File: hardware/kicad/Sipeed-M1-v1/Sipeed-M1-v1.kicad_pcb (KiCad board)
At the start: 2 copper layers, 161 parts, among them IC1 TROPIC01_chip, J1 USB_C_, J2 JST Connector, J3 Conn_02x20_Odd_Even, J4 Conn_01x09_Pin, J5 Conn_02x03_Odd_Even, J7 Conn_01x30_Pin, SW1 SW_Push, SW10 SW_Push, SW11 SW_Push, SW12 SW_Push, SW13 SW_Push, SW14 SW_Push, SW15 SW_Push, SW16 SW_Push, SW2 SW_Push, SW3 SW_Push, SW4 SW_Push, SW5 SW_Push, SW6 SW_Push, SW7 SW_Push, SW8 SW_Push, SW9 SW_Push, U1 Sipeed-M1, U2 ESP32-S3-WROOM-1U-N8R8, U3 PAM2401YPADJ, U4 TPS63070RNMR, U5 MCP23017_SO, U6 BQ29700DSER, U7 USBLC6-2SC6, U8 MCP73871

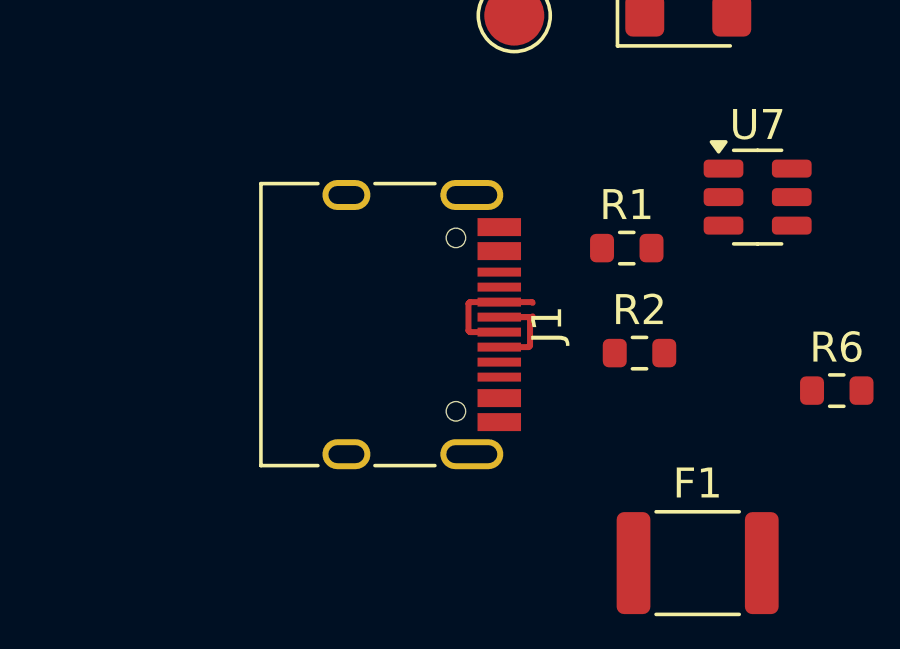
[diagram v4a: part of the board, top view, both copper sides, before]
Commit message: USB-C connector now using SHOU HAN TYPE-C 16PIN 2MD(073)
Adding footprint and 3D model.
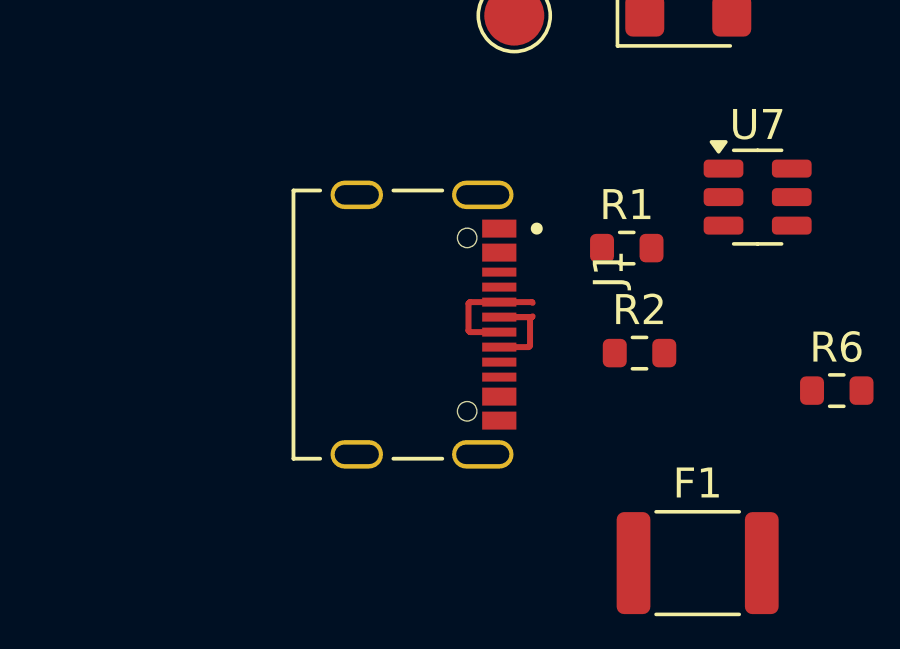
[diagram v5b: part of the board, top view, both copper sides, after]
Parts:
- J1: value USB_C_ -> USB_C; footprint Connector_USB:USB_C_Receptacle_HRO_TYPE-C-31-M-12 -> _M1_FP_lib:SHOUHAN_TYPE-C_16PIN_2MD__073_
- moved J1 0.37 mm to (103.8, 75.0)
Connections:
- J1 pad A8: (no net) -> unconnected-(J1-SBU1-PadA8)
- J1 pad B8: (no net) -> unconnected-(J1-SBU2-PadB8)

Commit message: New FPs for ESP32-S3, R1 and R2. Initial PCB routing.
Opted for ESP32-S3 with embedded PCB antenna.
R1 and R2 are now smaller to fit next to USB-C connector.
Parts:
- removed U6: BQ29700DSER, _M1_FP_lib:BQ29700_SON50P150X150X80-6N
- R1, R15, R2: footprint Resistor_SMD:R_0603_1608Metric -> Resistor_SMD:R_0402_1005Metric
- U2: value ESP32-S3-WROOM-1U-N8R8 -> ESP32-S3-WROOM-1-N4R8; footprint _M1_FP_lib:XCVR_ESP32-S3-WROOM-1U-N8R8-NU -> RF_Module:ESP32-S3-WROOM-1
- moved R23 95.2 mm to (129.2, 101.9)
- moved U8 94.2 mm to (127.3, 97.3)
- moved R22 93.4 mm to (129.7, 103.6)
- moved J2 92.9 mm to (113.2, 111.6), turned to -90 degrees
- moved R7 91.9 mm to (117.6, 93.0)
- moved C31 89.3 mm to (133.4, 98.1)
- moved U4 84.9 mm to (121.1, 96.0)
- moved C23 78.4 mm to (131.7, 184.9)
- moved R8 77.9 mm to (109.3, 104.0)
- moved L2 66.6 mm to (115.3, 102.2)
- moved C1 65.7 mm to (108.9, 72.1)
- moved JP9 65.3 mm to (134.1, 160.2)
- moved C3 63.8 mm to (124.8, 68.0)
- moved C19 60.9 mm to (110.4, 96.9)
- moved R25 59.9 mm to (114.0, 93.3)
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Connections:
- D3 pad 1: Net-(D3-A1) -> /VBUS_UP
- F1 pad 1: Net-(D3-A1) -> /VBUS_UP
- J1 pad A4: Net-(D3-A1) -> /VBUS_UP
- J1 pad A9: Net-(D3-A1) -> /VBUS_UP
- J1 pad B4: Net-(D3-A1) -> /VBUS_UP
- J1 pad B9: Net-(D3-A1) -> /VBUS_UP
- TP10 pad 1: Net-(D3-A1) -> /VBUS_UP
- U7 pad 4: unconnected-(U7-I/O2-Pad4) -> /USB_D+
- U7 pad 5: unconnected-(U7-VBUS-Pad5) -> /VBUS_UP
- U7 pad 6: unconnected-(U7-I/O1-Pad6) -> /USB_D-
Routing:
- net /VBUS_UP: track 0.00 -> 26.6 mm
- net /USB_D-: track 4.75 -> 27.6 mm, vias 0 -> 2
- net /USB_D+: track 4.12 -> 26.6 mm, vias 0 -> 2
- net GND: track 0.00 -> 21.3 mm, vias 0 -> 11
- net /PACK+: track 0.00 -> 11.9 mm
- net Net-(U8-PROG1): track 0.00 -> 8.08 mm
- net Net-(U8-PROG3): track 0.00 -> 4.93 mm
- net VBUS: track 0.00 -> 4.46 mm
- net Net-(J1-CC1): track 0.00 -> 1.69 mm
- net Net-(J1-CC2): track 0.00 -> 1.46 mm
- added copper zone on F.Cu, net GND
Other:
- board outline added: 89.4 x 67.4 mm
